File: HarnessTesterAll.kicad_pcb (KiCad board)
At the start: 2 copper layers, 38 parts, among them J1 Input Tester, J2 Output Tester, J3 JTAG, SW1 Reset, U1 PIC32MX110F016D-IPT

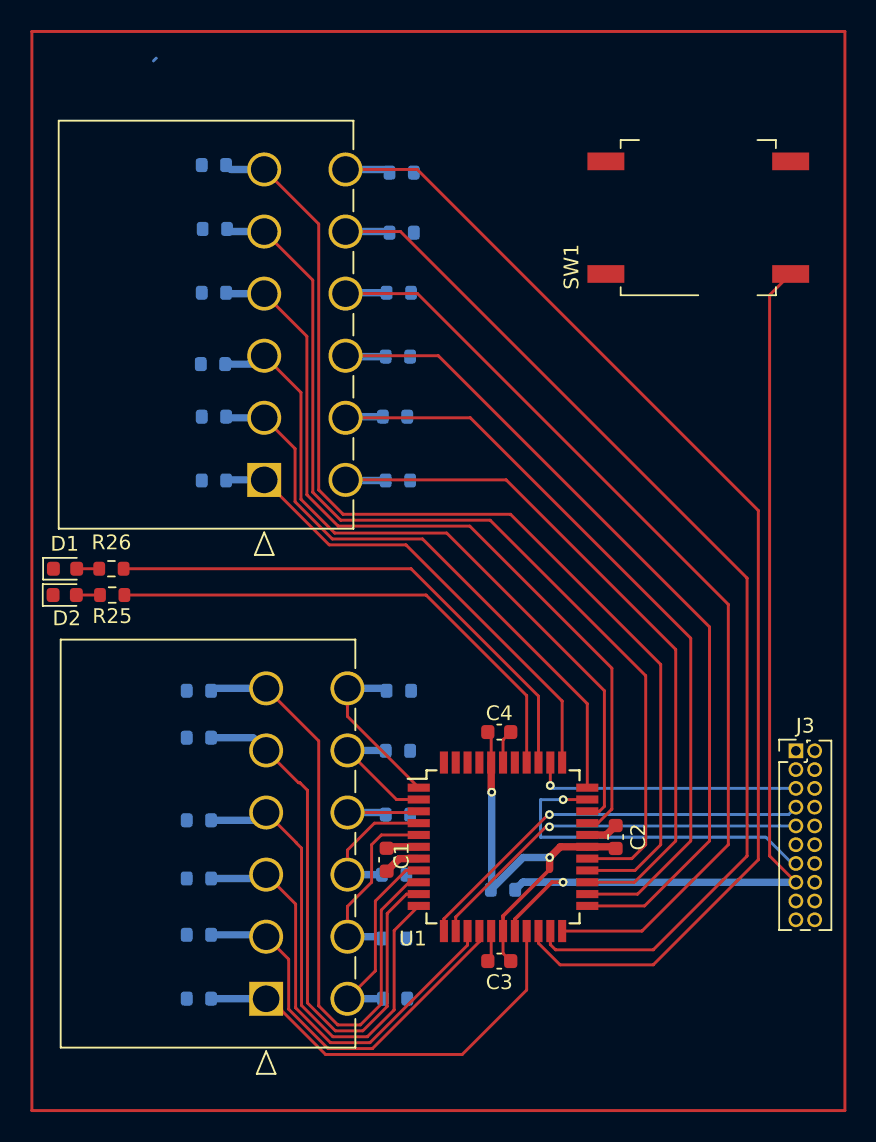
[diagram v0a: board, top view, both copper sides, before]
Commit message: Added board outline
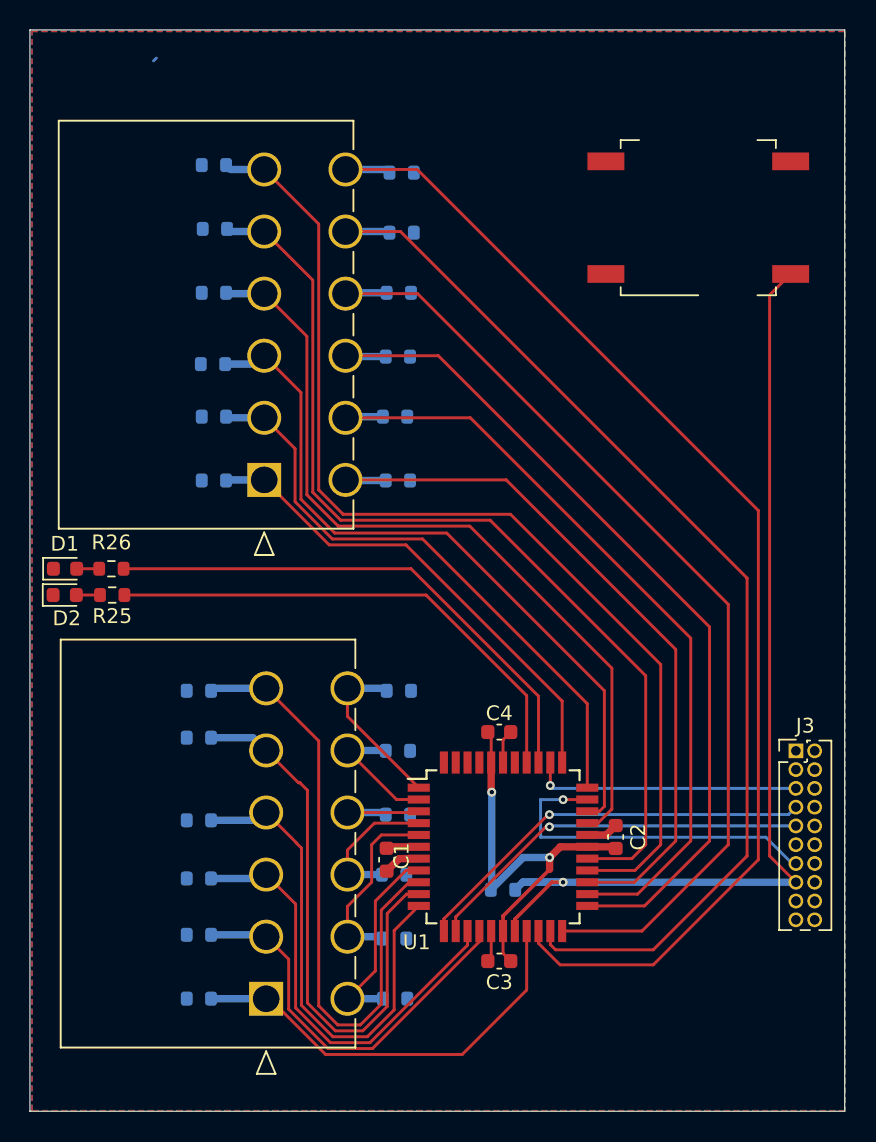
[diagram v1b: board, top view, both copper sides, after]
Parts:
- D1: value LED -> Good
- D2: value LED -> Bad
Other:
- board outline added: 55.1 x 73.2 mm
